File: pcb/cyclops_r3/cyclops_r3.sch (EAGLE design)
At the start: 47 parts, among them IC1 317-N, IC5 LM324, Q1 SUM11006, U1 ADR03, U2 OP1177

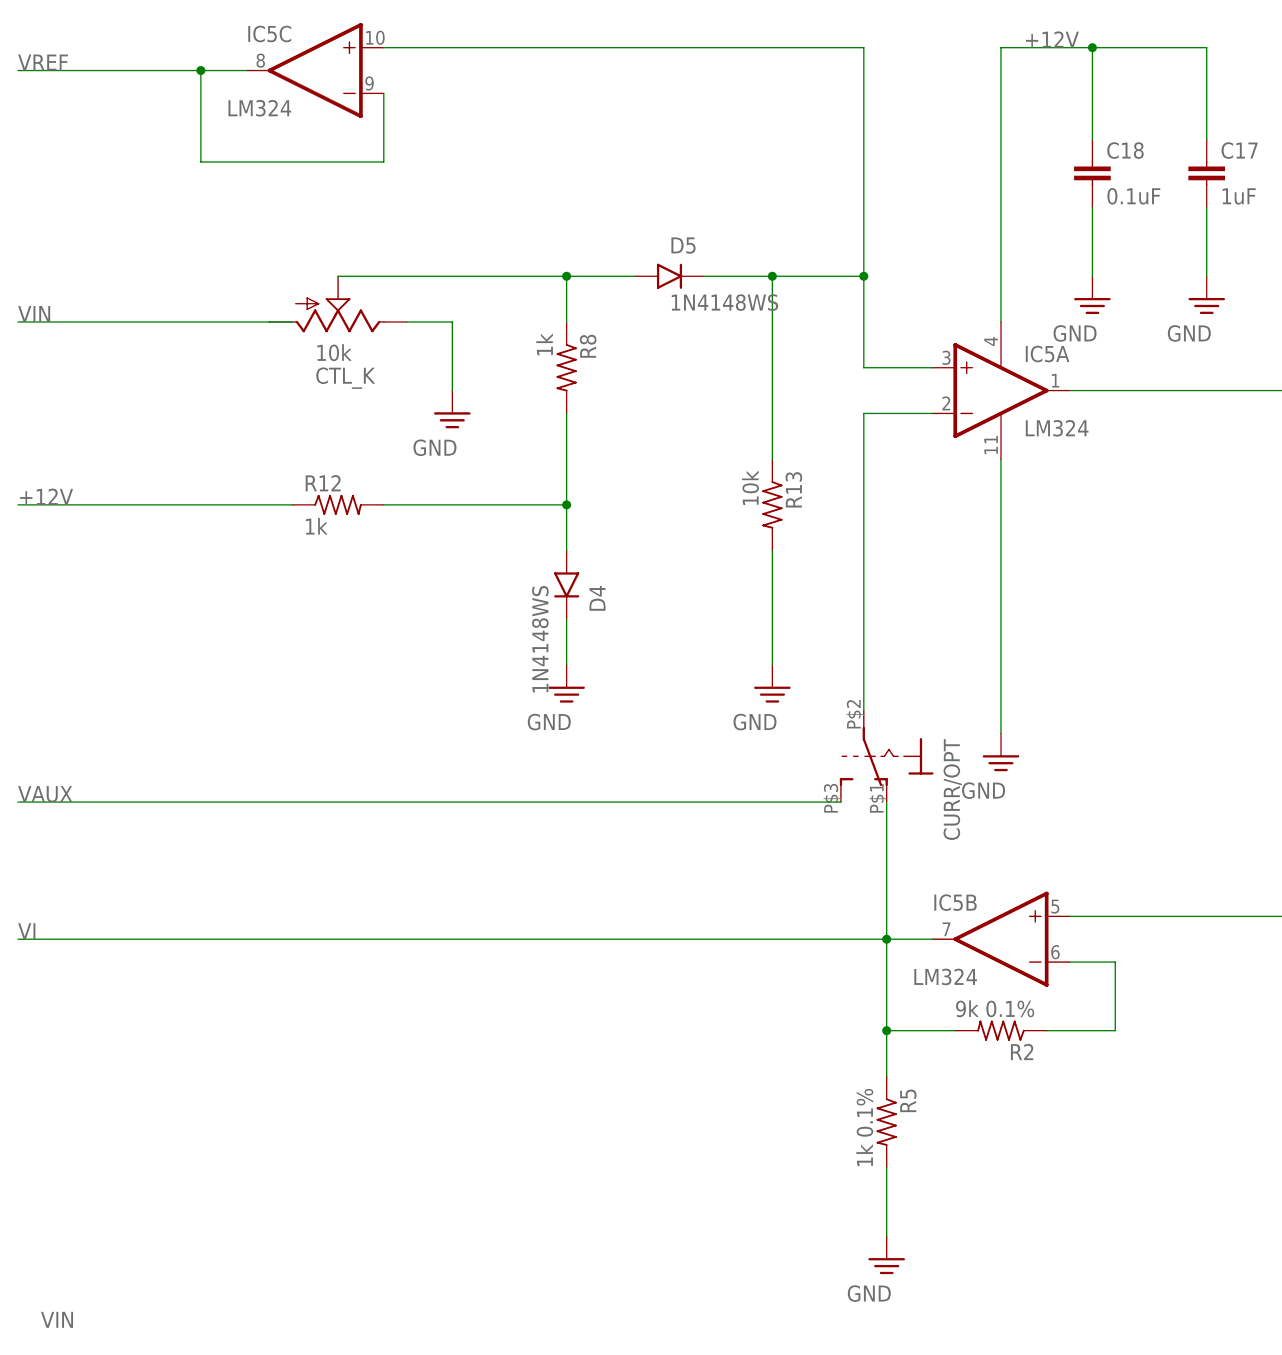
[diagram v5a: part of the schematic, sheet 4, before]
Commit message: Improved input diode clamp.
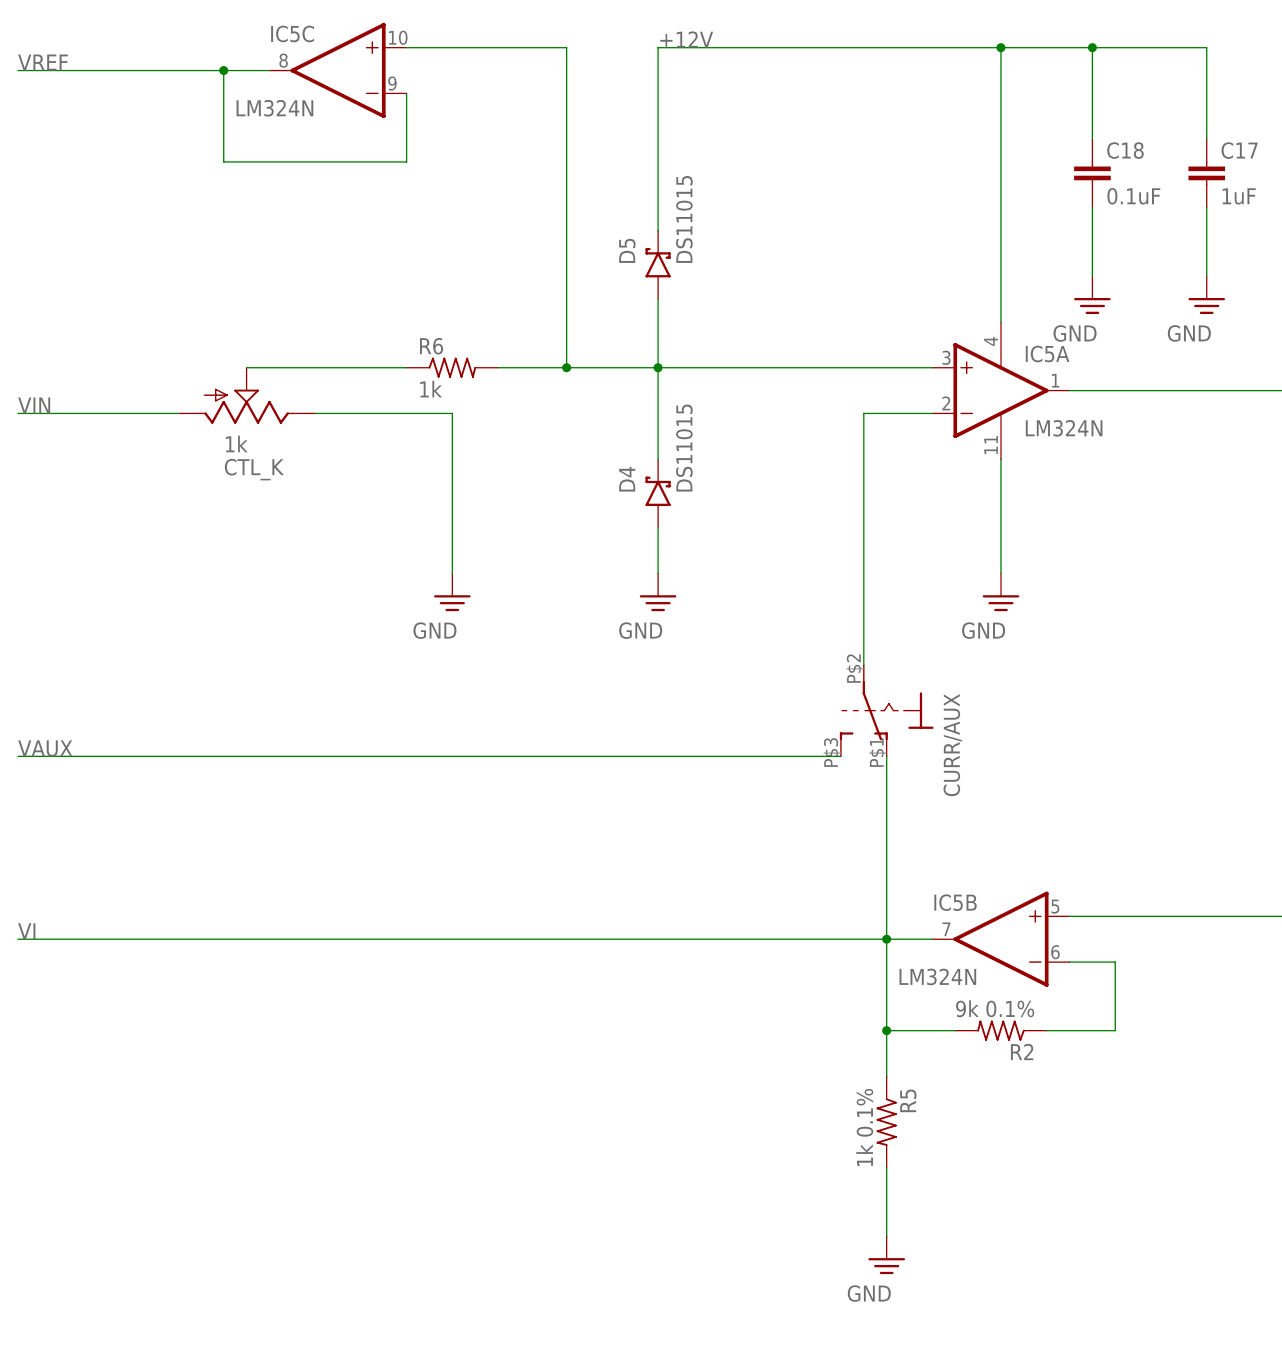
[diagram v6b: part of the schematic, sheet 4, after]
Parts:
- removed CURR/OPT: (no value), HOSS:SPST_SWITCH
- removed R12, R8: 1k, cyclops:R_0603
- removed R13: 10k, cyclops:R_0603
- added CURR/AUX: (no value), HOSS:SPST_SWITCH
- added R6: 1k, cyclops:R_0603
- CTL_K: value 10k -> 1k
- D4, D5: value 1N4148WS -> DS11015; device cyclops:DIODESOD-323F -> cyclops:S-DIODESOD-123
- I/O_BLOCK: value SCREW8 -> SCREW10_0.1-THRU; device cyclops:SCREW8 -> cyclops:SCREW10_0.1-THRU
- IC5: value LM324 -> LM324N
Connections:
- removed net BUFTEMP: I/O_BLOCK.8, U2.-IN, U2.OUT
- removed net N$5: D4.A, R12.2, R8.2
- new net VTEMP: I/O_BLOCK.9, U2.-IN, U2.OUT
- new net _VIN: D4.C, D5.A, IC5A.+IN, IC5C.+IN, R6.2
- net +12V: now also D5.C; no longer R12.1
- net GND: now also D4.A, I/O_BLOCK.10; no longer D4.C, R13.2
- net N$7: now also R6.1; no longer D5.A, R8.1
- net VAUX: now also CURR/AUX.S, I/O_BLOCK.8; no longer CURR/OPT.S, I/O_BLOCK.7
- net VFB: now also CURR/AUX.P; no longer CURR/OPT.P
- net VI: now also CURR/AUX.O, I/O_BLOCK.7; no longer CURR/OPT.O, I/O_BLOCK.6
- net VIN: now also I/O_BLOCK.5
- net VREF: now also I/O_BLOCK.6; no longer D5.C, I/O_BLOCK.5, IC5A.+IN, IC5C.+IN, R13.1
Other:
- moved on the sheet: CTL_K, IC5C

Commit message: Almost finished. Still trying to understand the best N-Channel MOSFET for sinking LED current.
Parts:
- removed CURR/AUX: (no value), HOSS:SPST_SWITCH
- added R8: 220k, cyclops:R_0603
- added S2: CURR/AUX, cyclops:SPDT_PCM12
- added S3: TEST, cyclops:SPDT_CFPA
- CTL_K: device HOSS:TRIM_US-RJ6S -> cyclops:TRIM_US-SM-42/43A
- REF_ADJ: device cyclops:TRIM_US-SM-42/43W -> cyclops:TRIM_US-SM-42/43A
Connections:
- net _VIN renamed _VREF
- removed net LED+: I/O_BLOCK.3
- new net VCTL: CTL_K.A, S3.2
- net +12V: now also I/O_BLOCK.3
- net DACA: now also S3.1
- net GND: now also R8.1
- net N$3: now also R8.2
- net VAUX: now also S2.3; no longer CURR/AUX.S
- net VFB: now also S2.2; no longer CURR/AUX.P
- net VI: now also S2.1, S3.3; no longer CURR/AUX.O
- net VIN: no longer CTL_K.A

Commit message: Started laying out board.
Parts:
- removed C17: 1uF, cyclops:C_0805
- removed C18: 0.1uF, cyclops:C_0603
- removed DAC: MCP4921, cyclops:MCP4921SOIC
- removed IC1: 317-N, cyclops:317_TO263
- removed IC5: LM324N, cyclops:LM324D
- added C2: 10uF, cyclops:C_0805
- added C3: 0.1uF, cyclops:C_0603
- added R12: (no value), cyclops:R_0603
- added U3: ADR03, cyclops:ADR03AKSZ-REEL7
- added U4: OP1177, cyclops:OP1177ARMZ
- added U5: LM324N, cyclops:LM324D
- added U6: DLD101, cyclops:DLD101
- C1: value 10uF -> ??; device cyclops:C_0805 -> cyclops:C_0603
- C10: device cyclops:C-POL_1206 -> cyclops:C_0805
- C11: value 10uF -> 0.1uF; device cyclops:C-POL_1206 -> cyclops:C_0603
- C12: value 47uF -> 0.1uF; device cyclops:C-POL_0807 -> cyclops:C_0603
- C13: value 1uF -> 0.1uF; device cyclops:C-POL_1206 -> cyclops:C_0603
- C14: value ?? -> 1uF; device cyclops:C_0603 -> cyclops:C_0805
- C5, C8: value 0.1uF -> 1uF; device cyclops:C_0603 -> cyclops:C-POL_1206
- C6: value 0.1uF -> 10uF; device cyclops:C_0603 -> cyclops:C-POL_1206
- C7: value 1uF -> 47uF; device cyclops:C_0805 -> cyclops:C-POL_0807
- D1: value S1B-13-F -> MMSZ5240B; device cyclops:DIODE-RECTS1B-13-F -> cyclops:Z-DIODE_MMSZ
- D3: value MMSZ5240B -> S1B-13-F; device cyclops:Z-DIODE_MMSZ -> cyclops:DIODE-RECTS1B-13-F
- R10: value 10k -> 120
- R11: value 240k -> 220k
- R2: value 9k 0.1% -> 10k
- R3: value 470 -> 1.8k
- R4: value 1k -> 240k
- R5: value 1k 0.1% -> 470
- R7: value 1.8k -> 1k
- R8: value 220k -> 1k 0.1%
- R9: value 120 -> 9k 0.1%
- REF_ADJ: device cyclops:TRIM_US-SM-42/43A -> cyclops:TRIM_US-SM-42/43W
- S1: value 219-04 -> TEST; device cyclops:219-04 -> cyclops:SPDT_CFPA
- S2: value CURR/AUX -> 219-04; device cyclops:SPDT_PCM12 -> cyclops:219-04
- S3: value TEST -> CURR/AUX; device cyclops:SPDT_CFPA -> cyclops:SPDT_PCM12
- U1: value ADR03 -> MCP4921; device cyclops:ADR03AKSZ-REEL7 -> cyclops:MCP4921SOIC
- U2: value OP1177 -> 317-N; device cyclops:OP1177ARMZ -> cyclops:317_TO263
- renumbered U$2 to U$1
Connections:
- removed net N$19: REF_ADJ.E
- new net AGND: C1.2, C10.2, C11.2, C12.2, C13.2, C14.2, C15.2, C2.2, C5.-, C6.-, C7.-, C8.-, C9.2, CTL_K.E, D5.A, I/O_BLOCK.10, I/O_BLOCK.2, R1.1, R10.1, R11.1, R2.1, R3.1, R6.1, R8.2, RSENSE.1, U3.GND, U4.V-, U5P.V-, U6.E
- new net N$5: R12.2, U6.C, U6.G
- new net N$6: R6.2, REF_ADJ.E
- net +12V: now also C10.1, C11.1, C12.1, C13.1, C7.+, C8.+, C9.1, D2.A, D3.C, D4.C, R12.1, R4.2, U2.VO, U3.VIN, U4.V+, U5P.V+; no longer C12.+, C13.+, C16.1, C17.1, C18.1, C4.1, C5.1, D1.A, D2.C, D5.C, IC1.VO, IC5P.V+, R11.2, U1.VIN, U2.V+
- net +15V: now also C5.+, D2.C, U2.VI; no longer C10.+, D3.C, IC1.VI
- net +5V: now also C3.1, C4.1, U1.VDD; no longer C8.1, C9.1, DAC.VDD
- net CS: now also S2.1, S2.2, S2.3, S2.4, U1.#CS; no longer DAC.#CS, S1.1, S1.2, S1.3, S1.4
- net CS0: now also S2.5; no longer S1.5
- net CS1: now also S2.6; no longer S1.6
- net CS2: now also S2.7; no longer S1.7
- net CS3: now also S2.8; no longer S1.8
- net DACA: now also C1.1, S1.1, U1.DACA; no longer C14.1, DAC.DACA, S3.1
- net GND: now also C3.2, U1.AVSS; no longer C1.2, C10.-, C11.-, C12.-, C13.-, C14.2, C15.2, C16.2, C17.2, C18.2, C5.2, C7.2, C8.2, C9.2, CTL_K.E, D4.A, DAC.AVSS, I/O_BLOCK.10, I/O_BLOCK.2, IC5P.V-, R1.1, R10.1, R5.2, R7.1, R8.1, R9.1, RSENSE.1, U1.GND, U2.V-
- net LDAC: now also U1.LDAC; no longer DAC.LDAC
- net LED-: now also U6.D
- net N$11: now also C14.1, C16.1, SJ1.1; no longer C6.1, C7.1, SJ1.2
- net N$15: now also R9.1, U5B.-IN; no longer IC5B.-IN, R2.1
- net N$18: now also D1.A, R2.2; no longer D3.A, R10.2
- net N$2: now also U5B.+IN, U6.S; no longer IC5B.+IN
- net N$20: now also R5.2, U3.TRIM; no longer R3.2, U1.TRIM
- net N$22: now also R5.1; no longer R3.1
- net N$3: now also R11.2, SJ1.2, U5A.OUT, U6.B; no longer IC5A.OUT, R8.2, SJ1.1
- net N$4: now also C16.2, R10.2; no longer C6.2, R9.2
- net N$7: now also R7.1; no longer R6.1
- net N$72: now also C6.+, D3.A, R3.2, R4.1, U2.ADJ; no longer C11.+, D2.A, IC1.ADJ, R11.1, R7.2
- net REFA: now also C2.1, U1.REFA, U3.VOUT; no longer C1.1, DAC.REFA, U1.VOUT
- net SCLK: now also U1.SCK; no longer DAC.SCK
- net SDI: now also U1.SDI; no longer DAC.SDI
- net TEMP: now also U3.TEMP, U4.+IN; no longer U1.TEMP, U2.+IN
- net VAUX: now also S3.3; no longer S2.3
- net VCTL: now also S1.2; no longer S3.2
- net VFB: now also S3.2, U5A.-IN; no longer IC5A.-IN, S2.2
- net VI: now also R8.1, R9.2, S1.3, S3.1, U5B.OUT; no longer IC5B.OUT, R2.2, R5.1, S2.1, S3.3
- net VREF: now also U5C.-IN, U5C.OUT; no longer IC5C.-IN, IC5C.OUT
- net VTEMP: now also U4.-IN, U4.OUT; no longer U2.-IN, U2.OUT
- net _VREF: now also D4.A, D5.C, R7.2, U5A.+IN, U5C.+IN; no longer D4.C, D5.A, IC5A.+IN, IC5C.+IN, R6.2
